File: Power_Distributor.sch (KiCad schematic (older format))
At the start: 2 parts

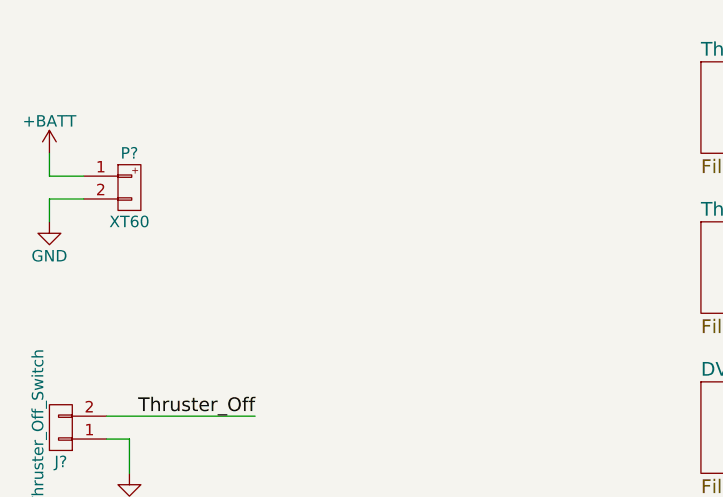
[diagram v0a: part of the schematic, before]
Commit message: Correct all foot-print assignments
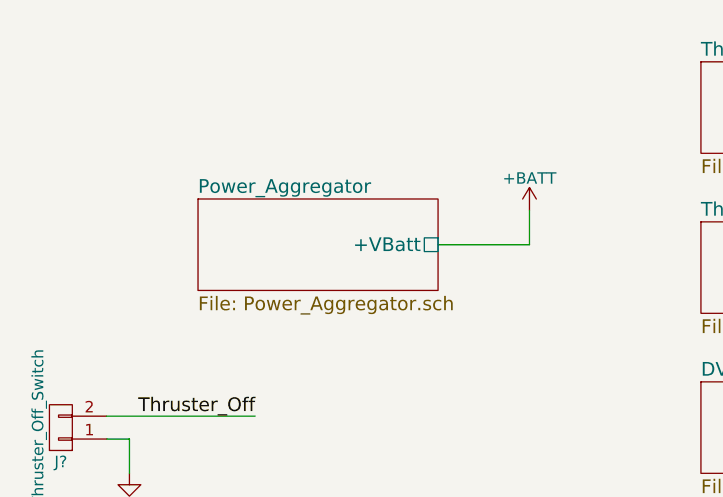
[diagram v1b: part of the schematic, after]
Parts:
- removed P?: XT60, symbol XT60
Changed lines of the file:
@@
 $Descr A4 11693 8268
 encoding utf-8
-Sheet 1 12
+Sheet 1 13
 Title ""
 Date ""
@@
 $EndSheet
 $Comp
-L XT60 P?
-U 1 1 58E5C87F
-P 2750 2200
-F 0 "P?" H 2750 2350 50  0000 C CNN
-F 1 "XT60" H 2750 2050 50  0000 C CNN
-F 2 "" H 2750 2200 60  0000 C CNN
-F 3 "" H 2750 2200 60  0000 C CNN
-	1    2750 2200
-	1    0    0    -1
-$EndComp
-$Comp
 L +BATT #PWR?
 U 1 1 58E61C00
-P 2400 2050
-F 0 "#PWR?" H 2400 1900 50  0001 C CNN
-F 1 "+BATT" H 2400 2190 50  0000 C CNN
-F 2 "" H 2400 2050 50  0001 C CNN
-F 3 "" H 2400 2050 50  0001 C CNN
-	1    2400 2050
-	1    0    0    -1
-$EndComp
-$Comp
-L GND #PWR?
-U 1 1 58E6205D
-P 2400 2350
-F 0 "#PWR?" H 2400 2100 50  0001 C CNN
-F 1 "GND" H 2400 2200 50  0000 C CNN
-F 2 "" H 2400 2350 50  0001 C CNN
-F 3 "" H 2400 2350 50  0001 C CNN
-	1    2400 2350
+P 4500 2300
+F 0 "#PWR?" H 4500 2150 50  0001 C CNN
+F 1 "+BATT" H 4500 2440 50  0000 C CNN
+F 2 "" H 4500 2300 50  0001 C CNN
+F 3 "" H 4500 2300 50  0001 C CNN
+	1    4500 2300
 	1    0    0    -1
 $EndComp
@@
 Text Label 6750 2650 2    60   ~ 0
 Thruster_Off
-Wire Wire Line
-	2400 2150 2550 2150
-Wire Wire Line
-	2550 2250 2400 2250
-Wire Wire Line
-	2400 2250 2400 2350
-Wire Wire Line
-	2400 2050 2400 2150
 Wire Wire Line
 	2650 3300 2750 3300
@@
 F17 "SW8_E" O R 8150 4050 60
 $EndSheet
+$Sheet
+S 3050 2250 1050 400
+U 58E5E8B2
+F0 "Power_Aggregator" 60
+F1 "Power_Aggregator.sch" 60
+F2 "+VBatt" U R 4100 2450 60
+$EndSheet
+Wire Wire Line
+	4100 2450 4500 2450
+Wire Wire Line
+	4500 2450 4500 2300
 $EndSCHEMATC

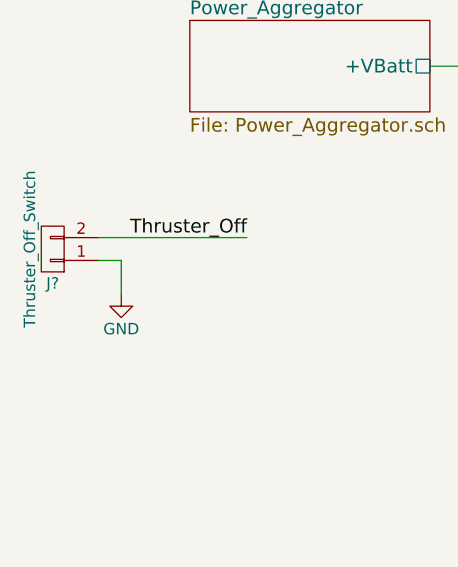
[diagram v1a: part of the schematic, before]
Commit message: Annotate all components
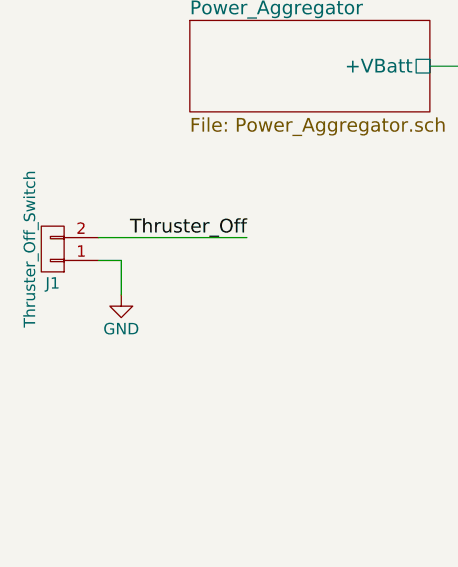
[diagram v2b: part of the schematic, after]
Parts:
- gave numbers to parts that had none: 1
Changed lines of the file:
@@
 LIBS:zeabus
 LIBS:ftdi
-LIBS:Power_Distributor-cache
 EELAYER 25 0
 EELAYER END
@@
 $EndSheet
 $Comp
-L +BATT #PWR?
+L +BATT #PWR01
 U 1 1 58E61C00
 P 4500 2300
-F 0 "#PWR?" H 4500 2150 50  0001 C CNN
+F 0 "#PWR01" H 4500 2150 50  0001 C CNN
 F 1 "+BATT" H 4500 2440 50  0000 C CNN
 F 2 "" H 4500 2300 50  0001 C CNN
@@
 $EndComp
 $Comp
-L CONN_01X02 J?
+L CONN_01X02 J1
 U 1 1 58E6ABEA
 P 2450 3250
-F 0 "J?" H 2450 3400 50  0000 C CNN
+F 0 "J1" H 2450 3400 50  0000 C CNN
 F 1 "Thruster_Off_Switch" V 2550 3250 50  0000 C CNN
 F 2 "" H 2450 3250 50  0001 C CNN
@@
 Thruster_Off
 $Comp
-L GND #PWR?
+L GND #PWR02
 U 1 1 58E6E6F3
 P 2750 3450
-F 0 "#PWR?" H 2750 3200 50  0001 C CNN
+F 0 "#PWR02" H 2750 3200 50  0001 C CNN
 F 1 "GND" H 2750 3300 50  0000 C CNN
 F 2 "" H 2750 3450 50  0001 C CNN
@@
 	8400 2650 9000 2650
 $Comp
-L +BATT #PWR?
+L +BATT #PWR03
 U 1 1 58EB597A
 P 6300 1650
-F 0 "#PWR?" H 6300 1500 50  0001 C CNN
+F 0 "#PWR03" H 6300 1500 50  0001 C CNN
 F 1 "+BATT" H 6300 1790 50  0000 C CNN
 F 2 "" H 6300 1650 50  0001 C CNN
@@
 	6300 1750 6150 1750
 $Comp
-L +BATT #PWR?
+L +BATT #PWR04
 U 1 1 58EB69B2
 P 6300 2350
-F 0 "#PWR?" H 6300 2200 50  0001 C CNN
+F 0 "#PWR04" H 6300 2200 50  0001 C CNN
 F 1 "+BATT" H 6300 2490 50  0000 C CNN
 F 2 "" H 6300 2350 50  0001 C CNN
@@
 	6300 2450 6150 2450
 $Comp
-L +BATT #PWR?
+L +BATT #PWR05
 U 1 1 58EB9A19
 P 6300 3050
-F 0 "#PWR?" H 6300 2900 50  0001 C CNN
+F 0 "#PWR05" H 6300 2900 50  0001 C CNN
 F 1 "+BATT" H 6300 3190 50  0000 C CNN
 F 2 "" H 6300 3050 50  0001 C CNN
@@
 	6300 3150 6150 3150
 $Comp
-L +BATT #PWR?
+L +BATT #PWR06
 U 1 1 58EBAA49
 P 6300 3750
-F 0 "#PWR?" H 6300 3600 50  0001 C CNN
+F 0 "#PWR06" H 6300 3600 50  0001 C CNN
 F 1 "+BATT" H 6300 3890 50  0000 C CNN
 F 2 "" H 6300 3750 50  0001 C CNN
@@
 	6300 3850 6300 3750
 $Comp
-L +BATT #PWR?
+L +BATT #PWR07
 U 1 1 58EBD7FB
 P 6300 4450
-F 0 "#PWR?" H 6300 4300 50  0001 C CNN
+F 0 "#PWR07" H 6300 4300 50  0001 C CNN
 F 1 "+BATT" H 6300 4590 50  0000 C CNN
 F 2 "" H 6300 4450 50  0001 C CNN
@@
 	6300 4550 6300 4450
 $Comp
-L +BATT #PWR?
+L +BATT #PWR08
 U 1 1 58EC0437
 P 8850 1650
-F 0 "#PWR?" H 8850 1500 50  0001 C CNN
+F 0 "#PWR08" H 8850 1500 50  0001 C CNN
 F 1 "+BATT" H 8850 1790 50  0000 C CNN
 F 2 "" H 8850 1650 50  0001 C CNN
@@
 	8850 1750 9000 1750
 $Comp
-L +BATT #PWR?
+L +BATT #PWR09
 U 1 1 58ECB208
 P 8850 2350
-F 0 "#PWR?" H 8850 2200 50  0001 C CNN
+F 0 "#PWR09" H 8850 2200 50  0001 C CNN
 F 1 "+BATT" H 8850 2490 50  0000 C CNN
 F 2 "" H 8850 2350 50  0001 C CNN
@@
 	8850 2450 9000 2450
 $Comp
-L +BATT #PWR?
+L +BATT #PWR010
 U 1 1 58ECC2C0
 P 8850 3050
-F 0 "#PWR?" H 8850 2900 50  0001 C CNN
+F 0 "#PWR010" H 8850 2900 50  0001 C CNN
 F 1 "+BATT" H 8850 3190 50  0000 C CNN
 F 2 "" H 8850 3050 50  0001 C CNN
@@
 	8850 3150 9000 3150
 $Comp
-L +BATT #PWR?
+L +BATT #PWR011
 U 1 1 58ECD1FA
 P 8850 3750
-F 0 "#PWR?" H 8850 3600 50  0001 C CNN
+F 0 "#PWR011" H 8850 3600 50  0001 C CNN
 F 1 "+BATT" H 8850 3890 50  0000 C CNN
 F 2 "" H 8850 3750 50  0001 C CNN
@@
 	8850 3850 9000 3850
 $Comp
-L +BATT #PWR?
+L +BATT #PWR012
 U 1 1 58ECE636
 P 8850 4450
-F 0 "#PWR?" H 8850 4300 50  0001 C CNN
+F 0 "#PWR012" H 8850 4300 50  0001 C CNN
 F 1 "+BATT" H 8850 4590 50  0000 C CNN
 F 2 "" H 8850 4450 50  0001 C CNN
